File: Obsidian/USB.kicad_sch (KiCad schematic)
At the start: 40 parts, among them J2 USB_C_Receptacle_USB2.0_16P, U21 FT2232HQ, U22 93LC46B_SN, U8 TLV62565DBV, Y5 X503212MSB2GI

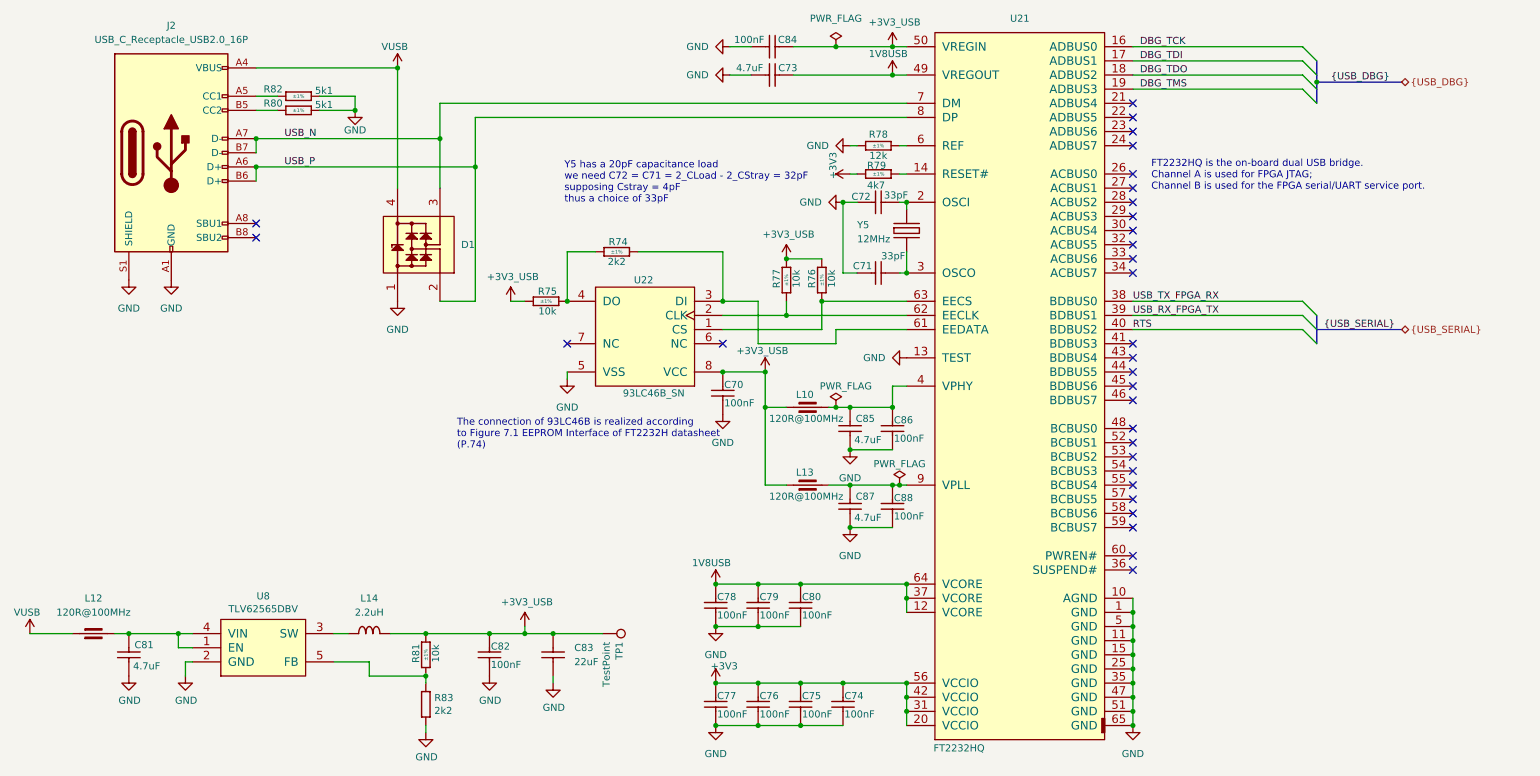
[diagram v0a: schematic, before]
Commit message: Cleaning symbol fields
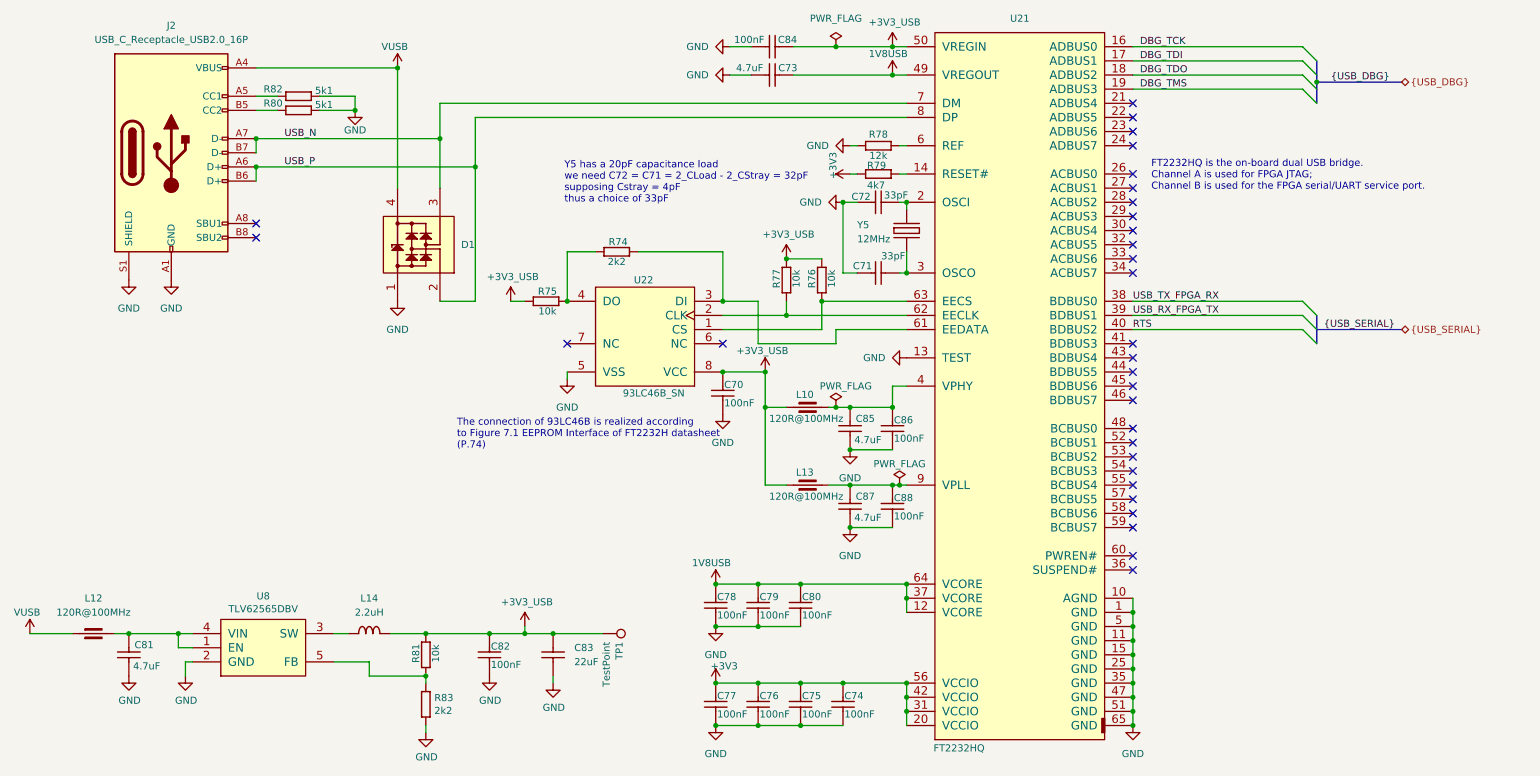
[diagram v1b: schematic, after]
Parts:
- C70, C74, C75, C76, C77, C78, C79, C80, C82, C84, C86, C88: Author CERN DEM MR -> (none); Case 0402 -> (none); Comment 100nF -> (none); Component Kind Standard -> (none); Component Type Standard -> (none); ComponentHeight (none) -> (none); CreateDate 06/30/17 00:00:00 -> (none); Database Table Name Capacitors -> (none); Footprint Library Capacitors SMD -> (none); Footprint Path PcbLib\Capacitors SMD.PcbLib -> (none); Footprint Ref CAPC1005X55N -> (none); HelpURL \\cern.ch\dfs\Applications\Altium\Datasheets\CC0402_MURATA_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 -> (none); LatestRevisionDate 06/30/17 00:00:00 -> (none); Library Name Capacitors SMD -> (none); Library Path SchLib\Capacitors.SchLib -> (none); Library Ref Capacitor - non polarized -> (none); License CC-BY-SA 4.0 -> (none); Manufacturer GENERIC -> (none); Manufacturer Part Number CC0402_100NF_50V_10%_X7R -> (none); Manufacturer1 ComponentHeight 0.55mm -> (none); Manufacturer1 Example MURATA -> (none); Manufacturer1 Part Number GRM155R71H104KE14D -> (none); Mounted Yes -> (none); PackageDescription (none) -> (none); Part Description SMD Multilayer Chip Ceramic Capacitor -> (none); Part Number CC0402_100NF_50V_10%_X7R -> (none); Pin Count 2 -> (none); PressFit (none) -> (none); SMD Yes -> (none); Sense No -> (none); Sense Comment (none) -> (none); Socket No -> (none); Status None -> (none); Status Comment (none) -> (none); TC X7R -> (none); Tolerance ±10% -> (none); Voltage 50V -> (none)
- C71: Author CERN DEM JLC -> (none); Case 0402 -> (none); Comment 33pF -> (none); Component Kind Standard -> (none); Component Type Standard -> (none); ComponentHeight (none) -> (none); CreateDate 10/25/12 00:00:00 -> (none); Database Table Name Capacitors -> (none); Footprint Library Capacitors SMD -> (none); Footprint Path PcbLib\Capacitors SMD.PcbLib -> (none); Footprint Ref CAPC1005X55N -> (none); HelpURL \\cern.ch\dfs\Applications\Altium\Datasheets\CC0402_C0G_KEM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 -> (none); LatestRevisionDate 04/22/15 00:00:00 -> (none); Library Name Capacitors SMD -> (none); Library Path SchLib\Capacitors.SchLib -> (none); Library Ref Capacitor - non polarized -> (none); License CC-BY-SA 4.0 -> (none); Manufacturer GENERIC -> (none); Manufacturer Part Number CC0402_33PF_50V_5%_C0G -> (none); Manufacturer1 ComponentHeight 0.55mm -> (none); Manufacturer1 Example Samsung Electro-Mechanics -> (none); Manufacturer1 Part Number CL05C330JB5NNNC -> (none); Mounted Yes -> (none); PackageDescription (none) -> (none); Part Description SMD Multilayer Chip Ceramic Capacitor -> (none); Part Number CC0402_33PF_50V_5%_C0G -> (none); Pin Count 2 -> (none); PressFit (none) -> (none); SMD Yes -> (none); Sense No -> (none); Sense Comment (none) -> (none); Socket No -> (none); Status Preferred -> (none); Status Comment (none) -> (none); TC C0G/NP0 -> (none); Tolerance ±5% -> (none); Voltage 50V -> (none)
- C72: Author CERN DEM JLC -> (none); Case 0402 -> (none); Comment 27pF -> (none); Component Kind Standard -> (none); Component Type Standard -> (none); ComponentHeight (none) -> (none); CreateDate 10/25/12 00:00:00 -> (none); Database Table Name Capacitors -> (none); Footprint Library Capacitors SMD -> (none); Footprint Path PcbLib\Capacitors SMD.PcbLib -> (none); Footprint Ref CAPC1005X55N -> (none); HelpURL \\cern.ch\dfs\Applications\Altium\Datasheets\CC0402_C0G_KEM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 -> (none); LatestRevisionDate 04/22/15 00:00:00 -> (none); Library Name Capacitors SMD -> (none); Library Path SchLib\Capacitors.SchLib -> (none); Library Ref Capacitor - non polarized -> (none); License CC-BY-SA 4.0 -> (none); Manufacturer GENERIC -> (none); Manufacturer Part Number CC0402_33PF_50V_5%_C0G -> (none); Manufacturer1 ComponentHeight 0.55mm -> (none); Manufacturer1 Example Samsung Electro-Mechanics -> (none); Manufacturer1 Part Number CL05C330JB5NNNC -> (none); Mounted Yes -> (none); PackageDescription (none) -> (none); Part Description SMD Multilayer Chip Ceramic Capacitor -> (none); Part Number CC0402_27PF_50V_5%_C0G -> (none); Pin Count 2 -> (none); PressFit (none) -> (none); SMD Yes -> (none); Sense No -> (none); Sense Comment (none) -> (none); Socket No -> (none); Status Preferred -> (none); Status Comment (none) -> (none); TC C0G/NP0 -> (none); Tolerance ±5% -> (none); Voltage 50V -> (none)
- C73, C81, C85, C87: Author CERN DEM BC -> (none); Case 0402 -> (none); Comment 4.7uF -> (none); Component Kind Standard -> (none); Component Type Standard -> (none); ComponentHeight (none) -> (none); CreateDate 09/07/20 00:00:00 -> (none); Database Table Name Capacitors -> (none); Footprint Library Capacitors SMD -> (none); Footprint Path PcbLib\Capacitors SMD.PcbLib -> (none); Footprint Ref CAPC1005X55N -> (none); HelpURL \\cern.ch\dfs\Applications\Altium\Datasheets\CC0402_X5R_YAG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 -> (none); LatestRevisionDate 09/07/20 00:00:00 -> (none); Library Name Capacitors SMD -> (none); Library Path SchLib\Capacitors.SchLib -> (none); Library Ref Capacitor - non polarized -> (none); License CC-BY-SA 4.0 -> (none); Manufacturer GENERIC -> (none); Manufacturer Part Number CC0402_4.7UF_16V_20%_X5R -> (none); Manufacturer1 ComponentHeight 0.55mm -> (none); Manufacturer1 Example YAGEO PHYCOMP -> (none); Manufacturer1 Part Number CC0402MRX5R7BB475 -> (none); Mounted Yes -> (none); PackageDescription (none) -> (none); Part Description SMD Multilayer Chip Ceramic Capacitor -> (none); Part Number CC0402_4.7UF_16V_20%_X5R -> (none); Pin Count 2 -> (none); PressFit (none) -> (none); SMD Yes -> (none); Sense No -> (none); Sense Comment (none) -> (none); Socket No -> (none); Status Preferred -> (none); Status Comment (none) -> (none); TC X5R -> (none); Tolerance ±20% -> (none); Voltage 16V -> (none)
- C83: Author CERN DEM JLC -> (none); Case 0805 -> (none); Comment 22uF -> (none); Component Kind Standard -> (none); Component Type Standard -> (none); ComponentHeight (none) -> (none); CreateDate 10/25/12 00:00:00 -> (none); Database Table Name Capacitors -> (none); Footprint Library Capacitors SMD -> (none); Footprint Path PcbLib\Capacitors SMD.PcbLib -> (none); Footprint Ref CAPC2012X135N -> (none); HelpURL \\cern.ch\dfs\Applications\Altium\Datasheets\CC0805_X5R_TDK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 -> (none); LatestRevisionDate 10/25/12 00:00:00 -> (none); Library Name Capacitors SMD -> (none); Library Path SchLib\Capacitors.SchLib -> (none); Library Ref Capacitor - non polarized -> (none); License CC-BY-SA 4.0 -> (none); Manufacturer GENERIC -> (none); Manufacturer Part Number CC0805_22UF_16V_10%_X5R -> (none); Manufacturer1 ComponentHeight 1.35mm -> (none); Manufacturer1 Example TDK -> (none); Manufacturer1 Part Number C2012X5R1C226KT -> (none); Mounted Yes -> (none); PackageDescription (none) -> (none); Part Description SMD Multilayer Chip Ceramic Capacitor -> (none); Part Number CC0805_22UF_16V_10%_X5R -> (none); Pin Count 2 -> (none); PressFit (none) -> (none); SMD Yes -> (none); Sense No -> (none); Sense Comment (none) -> (none); Socket No -> (none); Status Preferred -> (none); Status Comment (none) -> (none); TC X5R -> (none); Tolerance ±10% -> (none); Voltage 16V -> (none)
- D1: Author CERN DEM JLC -> (none); Bonding No -> (none); Case SOT143B -> (none); Comment PRTR5V0U2X -> (none); Component Kind Standard -> (none); Component Type Standard -> (none); ComponentHeight 1.1mm -> (none); ComponentLink1Description (none) -> (none); ComponentLink1URL (none) -> (none); ComponentLink2Description (none) -> (none); ComponentLink2URL (none) -> (none); CreateDate 03/22/11 00:00:00 -> (none); Database Table Name ICs And Semiconductors -> (none); Device PRTR5V0U2X -> (none); Field1 (none) -> (none); Footprint Library ICs And Semiconductors SMD -> (none); Footprint Path PcbLib\ICs And Semiconductors SMD.PcbLib -> (none); Footprint Ref SOT190P230X110-4N -> (none); HelpURL \\cern.ch\dfs\Applications\Altium\Datasheets\PRTR5V0U2X.pdf -> (none); LatestRevisionDate 03/22/11 00:00:00 -> (none); Library Name Diodes -> (none); Library Path SchLib\Diodes.SchLib -> (none); Library Ref PRTR5V0U2X -> (none); License CC-BY-SA 4.0 -> (none); Manufacturer NXP SEMICONDUCTORS -> (none); Manufacturer Part Number PRTR5V0U2X -> (none); Mounted Yes -> (none); PackageDescription SOT143B, SOT, 1.90mm Pitch; 4 Pin, 1.30mm W X 2.90mm L X 1.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 -> (none); Part Description Ultra Low Capacitance (1pF) Double Rail-to-Rail ESD Protect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 -> (none); Part Number PRTR5V0U2X -> (none); Pin Count 4 -> (none); Power (none) -> (none); PressFit No -> (none); SMD Yes -> (none); Sense No -> (none); Sense Comment (none) -> (none); Socket No -> (none); Status (none) -> (none); Status Comment (none) -> (none); Voltage 5.5V -> (none)
- L10, L12, L13: Author CERN DEM JMW -> (none); Case 0402 -> (none); Comment 120R@100MHz -> (none); Component Kind Standard -> (none); Component Type Standard -> (none); ComponentHeight 0.55mm -> (none); CreateDate 02/19/14 00:00:00 -> (none); Database Table Name Inductors & Transformers -> (none); Footprint Library Inductors SMD -> (none); Footprint Path PcbLib\Inductors SMD.PcbLib -> (none); Footprint Ref INDC1005X55N -> (none); HelpURL \\cern.ch\dfs\Applications\Altium\Datasheets\IND0402_MURATA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 -> (none); LatestRevisionDate 10/25/18 00:00:00 -> (none); Library Name Inductors SMD -> (none); Library Path SchLib\Inductors & Transformers.SchLib -> (none); Library Ref Ferrite Bead -> (none); License CC-BY-SA 4.0 -> (none); Manufacturer MURATA -> (none); Manufacturer Part Number BLM15PX121SN1D -> (none); Mounted Yes -> (none); PackageDescription (none) -> (none); Part Description SMD EMIFIL Chip Ferrite Bead -> (none); Part Number IND0402_MURATA_BLM15PX121SN1D -> (none); Pin Count 2 -> (none); Power 2A -> (none); Resistance 0.055R -> (none); SMD Yes -> (none); Sense No -> (none); Sense Comment (none) -> (none); Socket No -> (none); Status (none) -> (none); Status Comment (none) -> (none); Tolerance ±25% -> (none)
- L14: Author CERN DEM JLC -> (none); Case 0806 -> (none); Comment 2.2uH -> (none); Component Kind Standard -> (none); Component Type Standard -> (none); ComponentHeight 1mm -> (none); CreateDate 10/20/16 00:00:00 -> (none); Database Table Name Inductors & Transformers -> (none); Footprint Library Inductors SMD -> (none); Footprint Path PcbLib\Inductors SMD.PcbLib -> (none); Footprint Ref IND_WURTH_WE-PMCI_0806LR -> (none); HelpURL \\cern.ch\dfs\Applications\Altium\Datasheets\IND_WURTH_WE-P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 -> (none); LatestRevisionDate 10/20/16 00:00:00 -> (none); Library Name Inductors SMD -> (none); Library Path SchLib\Inductors & Transformers.SchLib -> (none); Library Ref Inductor -> (none); License CC-BY-SA 4.0 -> (none); Manufacturer WURTH ELEKTRONIK -> (none); Manufacturer Part Number 74479276222C -> (none); Mounted Yes -> (none); PackageDescription (none) -> (none); Part Description SMD Power Molded Chip Inductor (WE-PMCI Series) -> (none); Part Number IND_2.2UH_20%_WURTH_WE-PMCI_74479276222C -> (none); Pin Count 2 -> (none); Power 1.1A -> (none); Resistance 0.112R -> (none); SMD Yes -> (none); Sense No -> (none); Sense Comment (none) -> (none); Socket No -> (none); Status (none) -> (none); Status Comment (none) -> (none); Tolerance ±20% -> (none)
- R74: Author CERN DEM JLC -> (none); Case 0402 -> (none); Comment 2k2 -> (none); Component Kind Standard -> (none); Component Type Standard -> (none); ComponentHeight (none) -> (none); CreateDate 12/03/07 00:00:00 -> (none); Database Table Name Resistors -> (none); Footprint Library Resistors SMD -> (none); Footprint Path PcbLib\Resistors SMD.PcbLib -> (none); Footprint Ref RESC1005X40N -> (none); HelpURL \\cern.ch\dfs\Applications\Altium\Datasheets\R0402_Phycomp_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 -> (none); LatestRevisionDate 10/17/12 00:00:00 -> (none); Library Name Resistors SMD -> (none); Library Path SchLib\Resistors.SchLib -> (none); Library Ref Resistor - 1% -> (none); License CC-BY-SA 4.0 -> (none); Manufacturer GENERIC -> (none); Manufacturer Part Number R0402_2K2_1%_0.0625W_100PPM -> (none); Manufacturer1 ComponentHeight 0.4mm -> (none); Manufacturer1 Example YAGEO PHYCOMP -> (none); Manufacturer1 Part Number 232270672202L -> (none); Mounted Yes -> (none); PackageDescription (none) -> (none); Part Description General Purpose Thick Film Chip Resistor -> (none); Part Number R0402_2K2_1%_0.0625W_100PPM -> (none); Pin Count 2 -> (none); Power 0.0625W -> (none); PressFit No -> (none); SMD Yes -> (none); Sense No -> (none); Sense Comment (none) -> (none); Socket No -> (none); Status Not Recommended -> (none); Status Comment (none) -> (none); TC ±100ppm/°C -> (none); Tolerance ±1% -> (none); Voltage (none) -> (none)
- R75, R76, R77, R81: Author CERN DEM JLC -> (none); Case 0402 -> (none); Comment 10k -> (none); Component Kind Standard -> (none); Component Type Standard -> (none); ComponentHeight (none) -> (none); CreateDate 12/03/07 00:00:00 -> (none); Database Table Name Resistors -> (none); Footprint Library Resistors SMD -> (none); Footprint Path PcbLib\Resistors SMD.PcbLib -> (none); Footprint Ref RESC1005X40N -> (none); HelpURL \\cern.ch\dfs\Applications\Altium\Datasheets\R0402_Phycomp_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 -> (none); LatestRevisionDate 10/17/12 00:00:00 -> (none); Library Name Resistors SMD -> (none); Library Path SchLib\Resistors.SchLib -> (none); Library Ref Resistor - 1% -> (none); License CC-BY-SA 4.0 -> (none); Manufacturer GENERIC -> (none); Manufacturer Part Number R0402_10K_1%_0.0625W_100PPM -> (none); Manufacturer1 ComponentHeight 0.4mm -> (none); Manufacturer1 Example YAGEO PHYCOMP -> (none); Manufacturer1 Part Number 232270671003L -> (none); Mounted Yes -> (none); PackageDescription (none) -> (none); Part Description General Purpose Thick Film Chip Resistor -> (none); Part Number R0402_10K_1%_0.0625W_100PPM -> (none); Pin Count 2 -> (none); Power 0.0625W -> (none); PressFit No -> (none); SMD Yes -> (none); Sense No -> (none); Sense Comment (none) -> (none); Socket No -> (none); Status Not Recommended -> (none); Status Comment (none) -> (none); TC ±100ppm/°C -> (none); Tolerance ±1% -> (none); Voltage (none) -> (none)
- R78: Author CERN DEM JLC -> (none); Case 0402 -> (none); Comment 12k -> (none); Component Kind Standard -> (none); Component Type Standard -> (none); ComponentHeight (none) -> (none); CreateDate 12/03/07 00:00:00 -> (none); Database Table Name Resistors -> (none); Footprint Library Resistors SMD -> (none); Footprint Path PcbLib\Resistors SMD.PcbLib -> (none); Footprint Ref RESC1005X40N -> (none); HelpURL \\cern.ch\dfs\Applications\Altium\Datasheets\R0402_Phycomp_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 -> (none); LatestRevisionDate 10/17/12 00:00:00 -> (none); Library Name Resistors SMD -> (none); Library Path SchLib\Resistors.SchLib -> (none); Library Ref Resistor - 1% -> (none); License CC-BY-SA 4.0 -> (none); Manufacturer GENERIC -> (none); Manufacturer Part Number R0402_12K_1%_0.0625W_100PPM -> (none); Manufacturer1 ComponentHeight 0.4mm -> (none); Manufacturer1 Example YAGEO PHYCOMP -> (none); Manufacturer1 Part Number 232270671203L -> (none); Mounted Yes -> (none); PackageDescription (none) -> (none); Part Description General Purpose Thick Film Chip Resistor -> (none); Part Number R0402_12K_1%_0.0625W_100PPM -> (none); Pin Count 2 -> (none); Power 0.0625W -> (none); PressFit No -> (none); SMD Yes -> (none); Sense No -> (none); Sense Comment (none) -> (none); Socket No -> (none); Status Not Recommended -> (none); Status Comment (none) -> (none); TC ±100ppm/°C -> (none); Tolerance ±1% -> (none); Voltage (none) -> (none)
- R79: Author CERN DEM JLC -> (none); Case 0402 -> (none); Comment 4k7 -> (none); Component Kind Standard -> (none); Component Type Standard -> (none); ComponentHeight (none) -> (none); CreateDate 12/03/07 00:00:00 -> (none); Database Table Name Resistors -> (none); Footprint Library Resistors SMD -> (none); Footprint Path PcbLib\Resistors SMD.PcbLib -> (none); Footprint Ref RESC1005X40N -> (none); HelpURL \\cern.ch\dfs\Applications\Altium\Datasheets\R0402_Phycomp_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 -> (none); LatestRevisionDate 10/17/12 00:00:00 -> (none); Library Name Resistors SMD -> (none); Library Path SchLib\Resistors.SchLib -> (none); Library Ref Resistor - 1% -> (none); License CC-BY-SA 4.0 -> (none); Manufacturer GENERIC -> (none); Manufacturer Part Number R0402_4K7_1%_0.0625W_100PPM -> (none); Manufacturer1 ComponentHeight 0.4mm -> (none); Manufacturer1 Example YAGEO PHYCOMP -> (none); Manufacturer1 Part Number 232270674702L -> (none); Mounted Yes -> (none); PackageDescription (none) -> (none); Part Description General Purpose Thick Film Chip Resistor -> (none); Part Number R0402_4K7_1%_0.0625W_100PPM -> (none); Pin Count 2 -> (none); Power 0.0625W -> (none); PressFit No -> (none); SMD Yes -> (none); Sense No -> (none); Sense Comment (none) -> (none); Socket No -> (none); Status Not Recommended -> (none); Status Comment (none) -> (none); TC ±100ppm/°C -> (none); Tolerance ±1% -> (none); Voltage (none) -> (none)
- R80, R82: Author CERN DEM JLC -> (none); Case 0402 -> (none); Comment 5k1 -> (none); Component Kind Standard -> (none); Component Type Standard -> (none); ComponentHeight (none) -> (none); CreateDate 12/03/07 00:00:00 -> (none); Database Table Name Resistors -> (none); Footprint Library Resistors SMD -> (none); Footprint Path PcbLib\Resistors SMD.PcbLib -> (none); Footprint Ref RESC1005X40N -> (none); HelpURL \\cern.ch\dfs\Applications\Altium\Datasheets\R0402_Phycomp_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 -> (none); LatestRevisionDate 10/17/12 00:00:00 -> (none); Library Name Resistors SMD -> (none); Library Path SchLib\Resistors.SchLib -> (none); Library Ref Resistor - 1% -> (none); License CC-BY-SA 4.0 -> (none); Manufacturer GENERIC -> (none); Manufacturer Part Number R0402_5K1_1%_0.0625W_100PPM -> (none); Manufacturer1 ComponentHeight 0.4mm -> (none); Manufacturer1 Example YAGEO PHYCOMP -> (none); Manufacturer1 Part Number 232270675102L -> (none); Mounted Yes -> (none); PackageDescription (none) -> (none); Part Description General Purpose Thick Film Chip Resistor -> (none); Part Number R0402_5K1_1%_0.0625W_100PPM -> (none); Pin Count 2 -> (none); Power 0.0625W -> (none); PressFit No -> (none); SMD Yes -> (none); Sense No -> (none); Sense Comment (none) -> (none); Socket No -> (none); Status Not Recommended -> (none); Status Comment (none) -> (none); TC ±100ppm/°C -> (none); Tolerance ±1% -> (none); Voltage (none) -> (none)
- R83: Case 0402 -> (none); Comment =Value -> (none); Component Kind Standard -> (none); Component Type Standard -> (none); ComponentHeight (none) -> (none); CreateDate 12/03/07 00:00:00 -> (none); Database Table Name Resistors -> (none); Footprint Library Resistors SMD -> (none); Footprint Path PcbLib\Resistors SMD.PcbLib -> (none); Footprint Ref RESC1005X40N -> (none); HelpURL \\cern.ch\dfs\Applications\Altium\Datasheets\R0402_Phycomp_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 -> (none); LatestRevisionDate 10/17/12 00:00:00 -> (none); Library Name Resistors SMD -> (none); Library Path SchLib\Resistors.SchLib -> (none); Library Ref Resistor - 1% -> (none); License This work is licensed under the Creative Commons CC-BY-SA 4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 -> (none); Manufacturer GENERIC -> (none); Manufacturer Part Number R0402_2K2_1%_0.0625W_100PPM -> (none); Manufacturer1 ComponentHeight 0.4mm -> (none); Manufacturer1 Example YAGEO PHYCOMP -> (none); Manufacturer1 Part Number 232270672202L -> (none); Mounted Yes -> (none); PackageDescription (none) -> (none); Part Description General Purpose Thick Film Chip Resistor -> (none); Part Number R0402_2K2_1%_0.0625W_100PPM -> (none); Pin Count 2 -> (none); Power 0.0625W -> (none); PressFit No -> (none); SMD Yes -> (none); Sense No -> (none); Sense Comment (none) -> (none); Socket No -> (none); Status Not Recommended -> (none); Status Comment (none) -> (none); TC ±100ppm/°C -> (none); Tolerance ±1% -> (none); Voltage (none) -> (none)
- U21: Author CERN DEM JLC -> (none); Bonding No -> (none); Case QFN64 -> (none); Comment FT2232HQ -> (none); Component Kind Standard -> (none); Component Type Standard -> (none); ComponentHeight 1mm -> (none); ComponentLink1Description (none) -> (none); ComponentLink1URL (none) -> (none); ComponentLink2Description (none) -> (none); ComponentLink2URL (none) -> (none); CreateDate 11/12/14 00:00:00 -> (none); Database Table Name ICs And Semiconductors -> (none); Device FT2232HQ -> (none); Footprint Library ICs And Semiconductors SMD -> (none); Footprint Path PcbLib\ICs And Semiconductors SMD.PcbLib -> (none); Footprint Ref QFN50P900X900X100-65N-S445 -> (none); HelpURL \\cern.ch\dfs\Applications\Altium\Datasheets\FT2232HQ.pdf -> (none); LatestRevisionDate 11/12/14 00:00:00 -> (none); Library Name Analog & Interface -> (none); Library Path SchLib\Analog & Interface.SchLib -> (none); Library Ref FT2232HQ -> (none); License CC-BY-SA 4.0 -> (none); Manufacturer FUTURE TECHNOLOGY DEVICES INTERNATIONAL (FTDI) -> (none); Manufacturer Part Number FT2232HQ -> (none); Mounted Yes -> (none); PackageDescription QFN, 0.50mm Pitch, Square; 64 Pin, 9.00mm L X 9.00mm W X 1.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 -> (none); Part Description Dual High Speed USB To Multipurpose UART/FIFO IC -> (none); Part Number FT2232HQ -> (none); Pin Count 64 -> (none); PressFit No -> (none); SCEM (none) -> (none); SMD Yes -> (none); Sense No -> (none); Sense Comment (none) -> (none); Socket No -> (none); Status (none) -> (none); Status Comment (none) -> (none)
- U22: Author CERN DEM BC -> (none); Bonding No -> (none); Case SOIC8 -> (none); Comment 93C46B-I/SN -> (none); Component Kind Standard -> (none); Component Type Standard -> (none); ComponentHeight 1.75mm -> (none); ComponentLink1Description (none) -> (none); ComponentLink1URL (none) -> (none); ComponentLink2Description (none) -> (none); ComponentLink2URL (none) -> (none); CreateDate 02/14/20 00:00:00 -> (none); Database Table Name ICs And Semiconductors -> (none); Device 93C46B-I/SN -> (none); Footprint Library ICs And Semiconductors SMD -> (none); Footprint Path PcbLib\ICs And Semiconductors SMD.PcbLib -> (none); Footprint Ref SOIC127P600X175-8N -> (none); HelpURL \\cern.ch\dfs\Applications\Altium\Datasheets\93C46B-ISN.pdf -> (none); LatestRevisionDate 02/14/20 00:00:00 -> (none); Library Name Logic -> (none); Library Path SchLib\Logic.SchLib -> (none); Library Ref 93C46B-SN -> (none); License CC-BY-SA 4.0 -> (none); Manufacturer MICROCHIP TECHNOLOGY -> (none); Manufacturer Part Number 93C46B-I/SN -> (none); Mounted Yes -> (none); PackageDescription SOIC, 1.27mm Pitch; 8 Pin - Body 4x5mm, IPC Medium Density -> (none); Part Description 1Kbit, 5V, MICROWIRE® Serial EEPROM with 16-Bit Organization -> (none); Part Number 93C46B-I_SN -> (none); Pin Count 8 -> (none); PressFit No -> (none); SCEM (none) -> (none); SMD Yes -> (none); Sense No -> (none); Sense Comment (none) -> (none); Socket No -> (none); Status (none) -> (none); Status Comment (none) -> (none)
- U8: Case SOT23-5 -> (none); Comment =Device -> (none); Component Kind Standard -> (none); Component Type Standard -> (none); ComponentHeight 1.45mm -> (none); ComponentLink1Description (none) -> (none); ComponentLink2Description (none) -> (none); CreateDate 08/29/16 00:00:00 -> (none); Device TLV62565DBV -> (none); Footprint Path PcbLib\ICs And Semiconductors SMD.PcbLib -> (none); Footprint Ref SOT95P280X145-5N -> (none); LatestRevisionDate 08/29/16 00:00:00 -> (none); Library Name ICs And Semiconductors SMD -> (none); Library Path SchLib\Regulators.SchLib -> (none); Library Ref TLV62565 -> (none); License This work is licensed under the Creative Commons CC-BY-SA 4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 -> (none); Manufacturer TEXAS INSTRUMENTS -> (none); Manufacturer Part Number TLV62565DBVR -> (none); Mounted Yes -> (none); PackageDescription SOT, 0.95mm Pitch; 5 Pin, 1.60mm W X 2.90mm L X 1.45mm H Bo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 -> (none); Part Description 1.5A High Efficiency Step-Down Converter, Adjustable Output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 -> (none); Part Number TLV62565DBV -> (none); Pin Count 5 -> (none); PressFit No -> (none); SMD Yes -> (none); Sense No -> (none); Sense Comment (none) -> (none); Socket No -> (none); Status (none) -> (none); Status Comment (none) -> (none)
- Y5: Author CERN DEM JLC -> (none); Bonding No -> (none); Case (none) -> (none); Comment 12MHz -> (none); Component Kind Standard -> (none); Component Type Standard -> (none); ComponentHeight 1.2mm -> (none); ComponentLink1Description (none) -> (none); ComponentLink1URL (none) -> (none); ComponentLink2Description (none) -> (none); ComponentLink2URL (none) -> (none); CreateDate 11/12/14 00:00:00 -> (none); Database Table Name ICs And Semiconductors -> (none); Device (none) -> (none); Footprint Library ICs And Semiconductors SMD -> (none); Footprint Path PcbLib\ICs And Semiconductors SMD.PcbLib -> (none); Footprint Ref XTAL_TXC_7A -> (none); HelpURL \\cern.ch\dfs\Applications\Altium\Datasheets\XTAL_TXC_7A.pdf -> (none); LatestRevisionDate 11/12/14 00:00:00 -> (none); Library Name Crystals & Oscillators -> (none); Library Path SchLib\Crystals & Oscillators.SchLib -> (none); Library Ref Quartz Crystal -> (none); License CC-BY-SA 4.0 -> (none); Manufacturer TXC CORPORATION -> (none); Manufacturer Part Number 7A-12.000MAAJ-T -> (none); Mounted Yes -> (none); PackageDescription 2 Pins, 3.2x5mm, SMD Glass Seam Sealing Crystal, 7A Serie -> (none); Part Description Tolerance: ±30ppm, Stability: ±30ppm, -20°C to +70°C, 18pF,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 -> (none); Part Number X503212MSB2GI -> (none); Pin Count 2 -> (none); PressFit No -> (none); SMD Yes -> (none); Sense No -> (none); Sense Comment (none) -> (none); Socket No -> (none); Status (none) -> (none); Status Comment (none) -> (none)

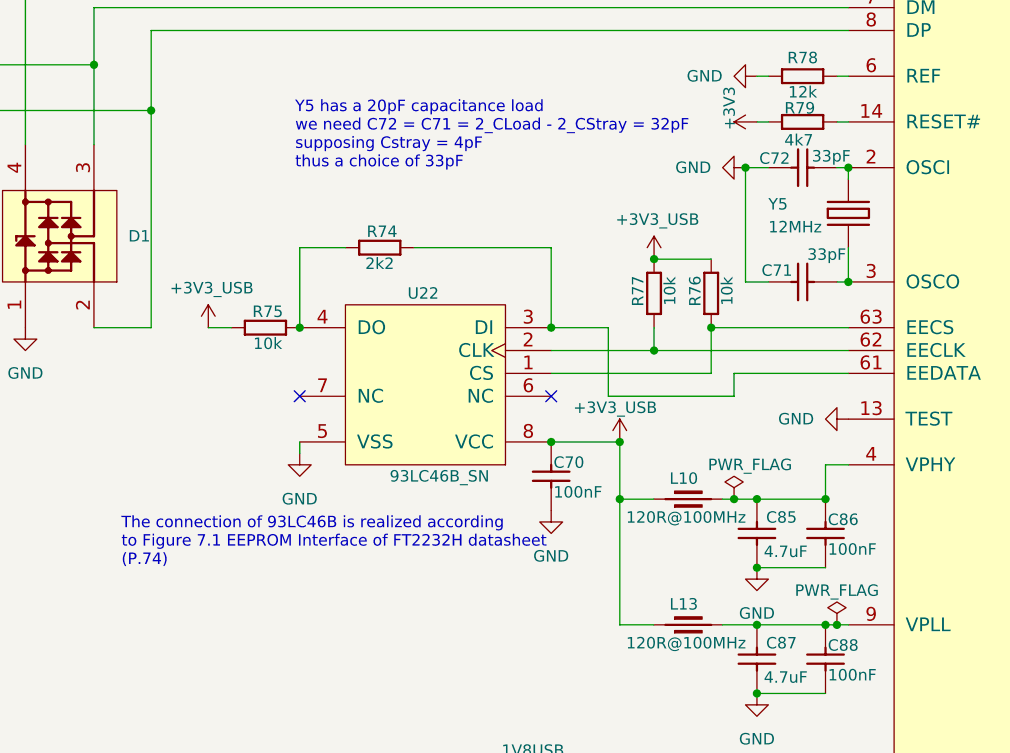
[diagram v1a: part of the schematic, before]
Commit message: cleaning zone around 93LC46B_SN (U22) in USB sheet
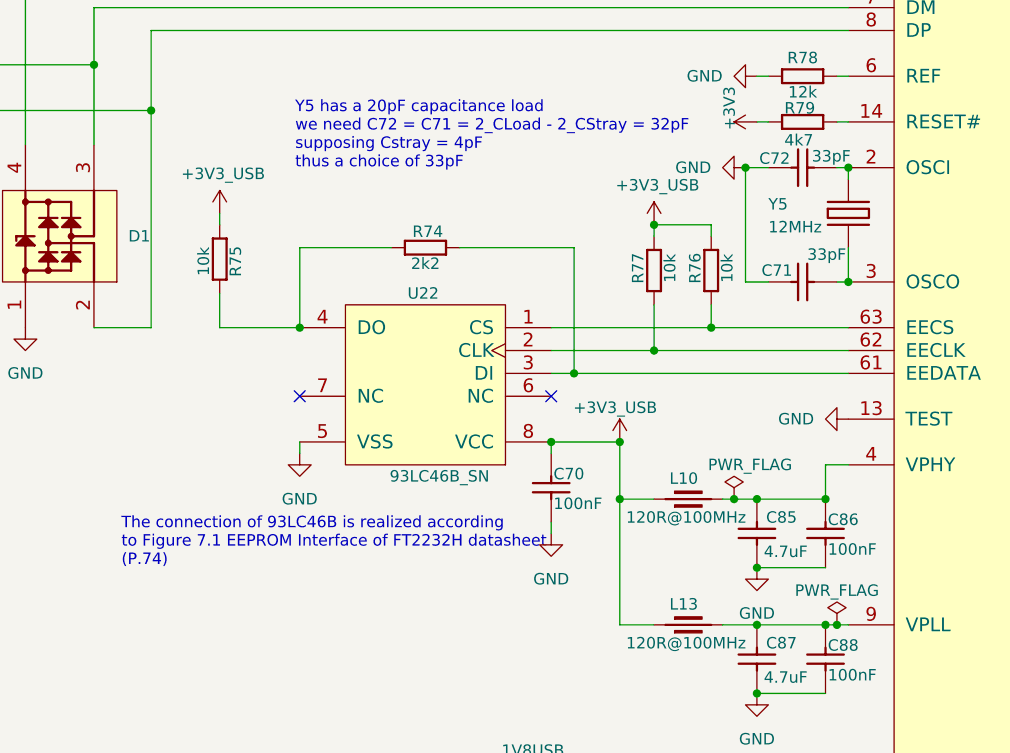
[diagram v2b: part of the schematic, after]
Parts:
- U22: footprint Footprint:SOIC127P600X175-8N -> ICs And Semiconductors SMD:SOIC127P600X175-8N; Author (none) -> CERN DEM BC; Bonding (none) -> No; Case (none) -> SOIC8; Comment (none) -> 93C46B-I/SN; Component Kind (none) -> Standard; Component Type (none) -> Standard; ComponentHeight (none) -> 1.75mm; ComponentLink1Description (none) -> (none); ComponentLink1URL (none) -> (none); ComponentLink2Description (none) -> (none); ComponentLink2URL (none) -> (none); CreateDate (none) -> 02/14/20 00:00:00; Database Table Name (none) -> ICs And Semiconductors; Device (none) -> 93C46B-I/SN; Footprint Library (none) -> ICs And Semiconductors SMD; Footprint Path (none) -> PcbLib\ICs And Semiconductors SMD.PcbLib; Footprint Ref (none) -> SOIC127P600X175-8N; HelpURL (none) -> \\cern.ch\dfs\Applications\Altium\Datasheets\93C46B-ISN.pdf; LatestRevisionDate (none) -> 02/14/20 00:00:00; Library Name (none) -> Logic; Library Path (none) -> SchLib\Logic.SchLib; Library Ref (none) -> 93C46B-SN; License (none) -> CC-BY-SA 4.0; Manufacturer (none) -> MICROCHIP TECHNOLOGY; Manufacturer Part Number (none) -> 93C46B-I/SN; Mounted (none) -> Yes; PackageDescription (none) -> SOIC, 1.27mm Pitch; 8 Pin - Body 4x5mm, IPC Medium Density; Part Description (none) -> 1Kbit, 5V, MICROWIRE® Serial EEPROM with 16-Bit Organization; Part Number (none) -> 93C46B-I_SN; Pin Count (none) -> 8; PressFit (none) -> No; SCEM (none) -> (none); SMD (none) -> Yes; Sense (none) -> No; Sense Comment (none) -> (none); Socket (none) -> No; Status (none) -> (none); Status Comment (none) -> (none)
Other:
- moved on the sheet: C70, R74, R75, R76, R77

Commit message: Clean symbol fields
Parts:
- U22: Author CERN DEM BC -> (none); Bonding No -> (none); Case SOIC8 -> (none); Comment 93C46B-I/SN -> (none); Component Kind Standard -> (none); Component Type Standard -> (none); ComponentHeight 1.75mm -> (none); ComponentLink1Description (none) -> (none); ComponentLink1URL (none) -> (none); ComponentLink2Description (none) -> (none); ComponentLink2URL (none) -> (none); CreateDate 02/14/20 00:00:00 -> (none); Database Table Name ICs And Semiconductors -> (none); Device 93C46B-I/SN -> (none); Footprint Library ICs And Semiconductors SMD -> (none); Footprint Path PcbLib\ICs And Semiconductors SMD.PcbLib -> (none); Footprint Ref SOIC127P600X175-8N -> (none); HelpURL \\cern.ch\dfs\Applications\Altium\Datasheets\93C46B-ISN.pdf -> (none); LatestRevisionDate 02/14/20 00:00:00 -> (none); Library Name Logic -> (none); Library Path SchLib\Logic.SchLib -> (none); Library Ref 93C46B-SN -> (none); License CC-BY-SA 4.0 -> (none); Manufacturer MICROCHIP TECHNOLOGY -> (none); Manufacturer Part Number 93C46B-I/SN -> (none); Mounted Yes -> (none); PackageDescription SOIC, 1.27mm Pitch; 8 Pin - Body 4x5mm, IPC Medium Density -> (none); Part Description 1Kbit, 5V, MICROWIRE® Serial EEPROM with 16-Bit Organization -> (none); Part Number 93C46B-I_SN -> (none); Pin Count 8 -> (none); PressFit No -> (none); SCEM (none) -> (none); SMD Yes -> (none); Sense No -> (none); Sense Comment (none) -> (none); Socket No -> (none); Status (none) -> (none); Status Comment (none) -> (none)

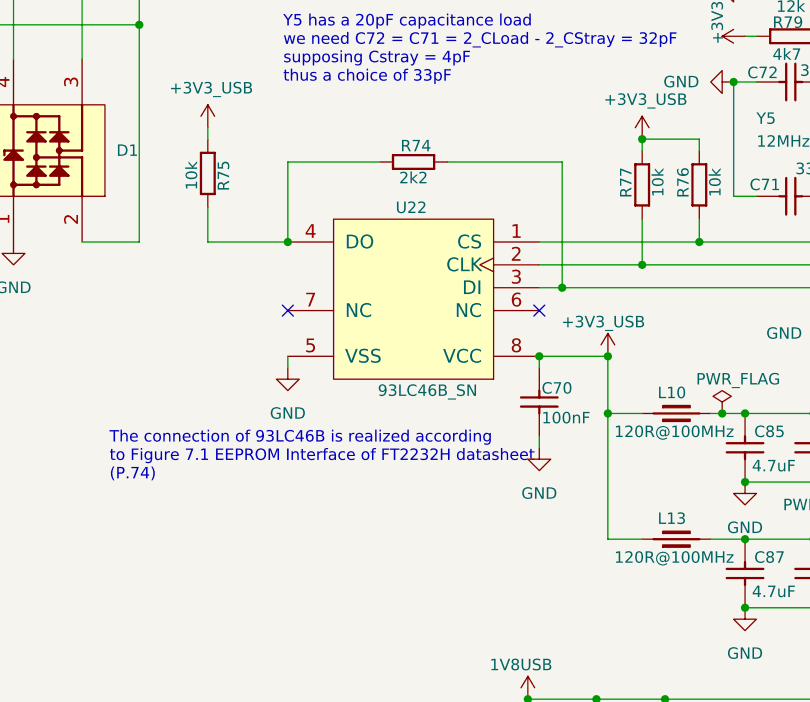
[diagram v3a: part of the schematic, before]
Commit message: adding resistor in SFP sheep for SFP/SFP+ compatibility
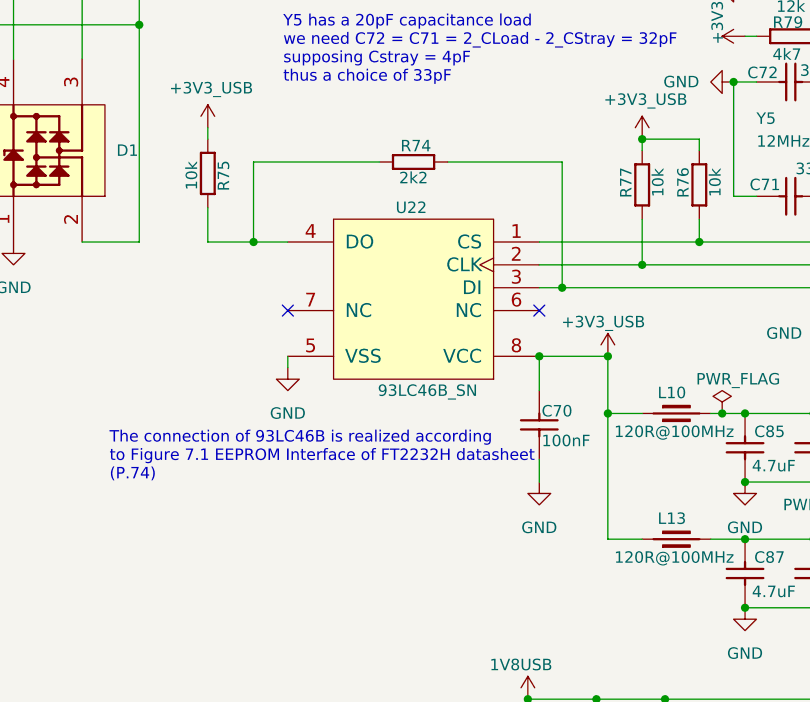
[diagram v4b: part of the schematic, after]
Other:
- moved on the sheet: C70
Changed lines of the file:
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@@
 	)
 	(junction
+		(at 116.84 74.93)
+		(diameter 0)
+		(color 0 0 0 0)
+	)
+	(junction
 		(at 147.32 125.73)
 		(diameter 0)
@@
 	)
 	(junction
-		(at 120.65 74.93)
-		(diameter 0)
-		(color 0 0 0 0)
-	)
-	(junction
 		(at 170.18 143.51)
 		(diameter 0)
@@
 	(wire
 		(pts
-			(xy 148.59 88.9) (xy 148.59 87.63)
+			(xy 148.59 91.44) (xy 148.59 87.63)
 		)
 		(stroke
@@
 	(wire
 		(pts
+			(xy 116.84 74.93) (xy 120.65 74.93)
+		)
+		(stroke
+			(width 0)
+			(type default)
+		)
+	)
+	(wire
+		(pts
 			(xy 180.34 52.07) (xy 181.61 52.07)
 		)
@@
 	(wire
 		(pts
-			(xy 130.81 66.04) (xy 120.65 66.04)
+			(xy 130.81 66.04) (xy 116.84 66.04)
 		)
 		(stroke
@@
 	(wire
 		(pts
-			(xy 120.65 66.04) (xy 120.65 74.93)
+			(xy 116.84 66.04) (xy 116.84 74.93)
 		)
 		(stroke
@@
 	(wire
 		(pts
-			(xy 148.59 97.79) (xy 148.59 96.52)
+			(xy 148.59 101.6) (xy 148.59 99.06)
 		)
 		(stroke
@@
 	(wire
 		(pts
-			(xy 111.76 74.93) (xy 120.65 74.93)
+			(xy 111.76 74.93) (xy 116.84 74.93)
 		)
 		(stroke
@@
 	(symbol
 		(lib_id "Library_Symbol:CC0402_100NF_50V_10%_X7R")
-		(at 148.59 96.52 90)
+		(at 148.59 99.06 90)
 		(unit 1)
 		(exclude_from_sim no)
@@
 		(dnp no)
 		(property "Reference" "C70"
-			(at 148.844 91.186 90)
+			(at 148.844 93.726 90)
 			(effects
 				(font
@@
 		)
 		(property "Value" "CC0402_100NF_50V_10%_X7R"
-			(at 154.813 96.52 0)
+			(at 154.813 99.06 0)
 			(effects
 				(font
@@
 		)
 		(property "Footprint" "Footprint:CAPC1005X55N"
-			(at 156.718 96.52 0)
+			(at 156.718 99.06 0)
 			(effects
 				(font
@@
 		)
 		(property "Datasheet" "\\\\cern.ch\\dfs\\Applications\\Altium\\Datasheets\\CC0402_MURATA_GRM155R71H104KE14D.pdf"
-			(at 158.623 96.52 0)
+			(at 158.623 99.06 0)
 			(effects
 				(font
@@
 		)
 		(property "Description" "SMD Multilayer Chip Ceramic Capacitor"
-			(at 148.59 96.52 0)
+			(at 148.59 99.06 0)
 			(effects
 				(font
@@
 		)
 		(property "Val" "100nF"
-			(at 148.844 94.488 90)
+			(at 148.844 97.028 90)
 			(effects
 				(font
@@
 		)
 		(property "FT Rotation Offset" ""
-			(at 148.59 96.52 90)
+			(at 148.59 99.06 90)
 			(effects
 				(font
@@
 		)
 		(property "LCSC" "C110251"
-			(at 148.59 96.52 90)
+			(at 148.59 99.06 90)
 			(effects
 				(font
@@
 	(symbol
 		(lib_id "Library_Symbol:GND")
-		(at 148.59 97.79 0)
+		(at 148.59 101.6 0)
 		(unit 1)
 		(exclude_from_sim no)
@@
 		(fields_autoplaced yes)
 		(property "Reference" "#PWR081"
-			(at 148.59 104.14 0)
+			(at 148.59 107.95 0)
 			(effects
 				(font
@@
 		)
 		(property "Value" "GND"
-			(at 148.59 102.87 0)
+			(at 148.59 106.68 0)
 			(effects
 				(font
@@
 		)
 		(property "Footprint" ""
-			(at 148.59 97.79 0)
+			(at 148.59 101.6 0)
 			(effects
 				(font
@@
 		)
 		(property "Datasheet" ""
-			(at 148.59 97.79 0)
+			(at 148.59 101.6 0)
 			(effects
 				(font
@@
 		)
 		(property "Description" "Power symbol creates a global label with name \"GND\" , ground"
-			(at 148.59 97.79 0)
+			(at 148.59 101.6 0)
 			(effects
 				(font
